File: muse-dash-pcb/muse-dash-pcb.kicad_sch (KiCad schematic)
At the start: 24 parts, among them SW0 CherryMX, SW1 CherryMX, SW1 SW_Push, SW2 CherryMX, SW3 CherryMX, U1 ATmega32U4-A, Y1 Crystal_GND24

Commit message: added footprints
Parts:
- C1: renamed from C2; footprint (none) -> Capacitor_SMD:C_0805_2012Metric
- C2: renamed from C6; footprint (none) -> Capacitor_SMD:C_0805_2012Metric
- C3: renamed from C7; footprint (none) -> Capacitor_SMD:C_0805_2012Metric
- C4: renamed from C3; footprint (none) -> Capacitor_SMD:C_0805_2012Metric
- C5: renamed from C4; footprint (none) -> Capacitor_SMD:C_0805_2012Metric
- C6: renamed from C1; footprint (none) -> Capacitor_SMD:C_0805_2012Metric
- C7: renamed from C5; footprint (none) -> Capacitor_SMD:C_0805_2012Metric
- D1: footprint (none) -> Diode_SMD:D_0805_2012Metric_Pad1.15x1.40mm_HandSolder
- D2: renamed from D3; footprint (none) -> Diode_SMD:D_0805_2012Metric_Pad1.15x1.40mm_HandSolder
- D3: renamed from D4; footprint (none) -> Diode_SMD:D_0805_2012Metric_Pad1.15x1.40mm_HandSolder
- D4: renamed from D2; footprint (none) -> Diode_SMD:D_0805_2012Metric_Pad1.15x1.40mm_HandSolder
- F1: footprint (none) -> Fuse:Fuse_1206_3216Metric_Pad1.42x1.75mm_HandSolder
- R1: renamed from R2; footprint (none) -> Resistor_SMD:R_0805_2012Metric_Pad1.20x1.40mm_HandSolder
- R2: renamed from R3; footprint (none) -> Resistor_SMD:R_0805_2012Metric_Pad1.20x1.40mm_HandSolder
- R3: renamed from R4; footprint (none) -> Resistor_SMD:R_0805_2012Metric_Pad1.20x1.40mm_HandSolder
- R4: renamed from R1; footprint (none) -> Resistor_SMD:R_0805_2012Metric_Pad1.20x1.40mm_HandSolder
- SW0: renamed from SW1; footprint (none) -> Button_Switch_SMD:SW_SPST_SKQG_WithStem
- SW1: renamed from SW0; footprint (none) -> Button_Switch_Keyboard:SW_Cherry_MX_1.00u_PCB
- SW2: renamed from SW1; footprint (none) -> Button_Switch_Keyboard:SW_Cherry_MX_1.00u_PCB
- SW3: renamed from SW2; footprint (none) -> Button_Switch_Keyboard:SW_Cherry_MX_1.00u_PCB
- SW4: renamed from SW3; footprint (none) -> Button_Switch_Keyboard:SW_Cherry_MX_1.00u_PCB
- Y1: footprint (none) -> Crystal:Crystal_SMD_3225-4Pin_3.2x2.5mm_HandSoldering
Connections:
- net SW1: now also U1.10 (PB2); no longer SW2.2, U1.11 (PB3)
- net SW2: now also SW2.2, U1.11 (PB3); no longer SW3.2, U1.28 (PB4)
- net SW3: now also SW3.2, U1.28 (PB4); no longer U1.29 (PB5)
- net SW0 renamed SW4
- net SW4: now also U1.29 (PB5); no longer U1.10 (PB2)

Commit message: completed pcb design
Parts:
- USB1: footprint (none) -> Connector_USB:USB_Mini-B_Lumberg_2486_01_Horizontal
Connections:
- net COM: now also U1.22 (PD5)
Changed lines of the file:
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@@
+		)
+	)
+	(global_label "COM"
+		(shape input)
+		(at 91.44 132.08 0)
+		(fields_autoplaced yes)
+		(effects
+			(font
+				(size 1.27 1.27)
+			)
+			(justify left)
+		)
+		(property "Intersheetrefs" "${INTERSHEET_REFS}"
+			(at 98.4771 132.08 0)
+			(effects
+				(font
+					(size 1.27 1.27)
+				)
+				(justify left)
+				(hide yes)
+			)
 		)
 	)
@@
 			)
 		)
-		(property "Footprint" ""
+		(property "Footprint" "Connector_USB:USB_Mini-B_Lumberg_2486_01_Horizontal"
 			(at 238.76 34.29 0)
 			(effects

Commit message: fixed routes and added mounting holes
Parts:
- added H1, H2, H3, H4: MountingHole, MountingHole:MountingHole_2.1mm, symbol Mechanical:MountingHole

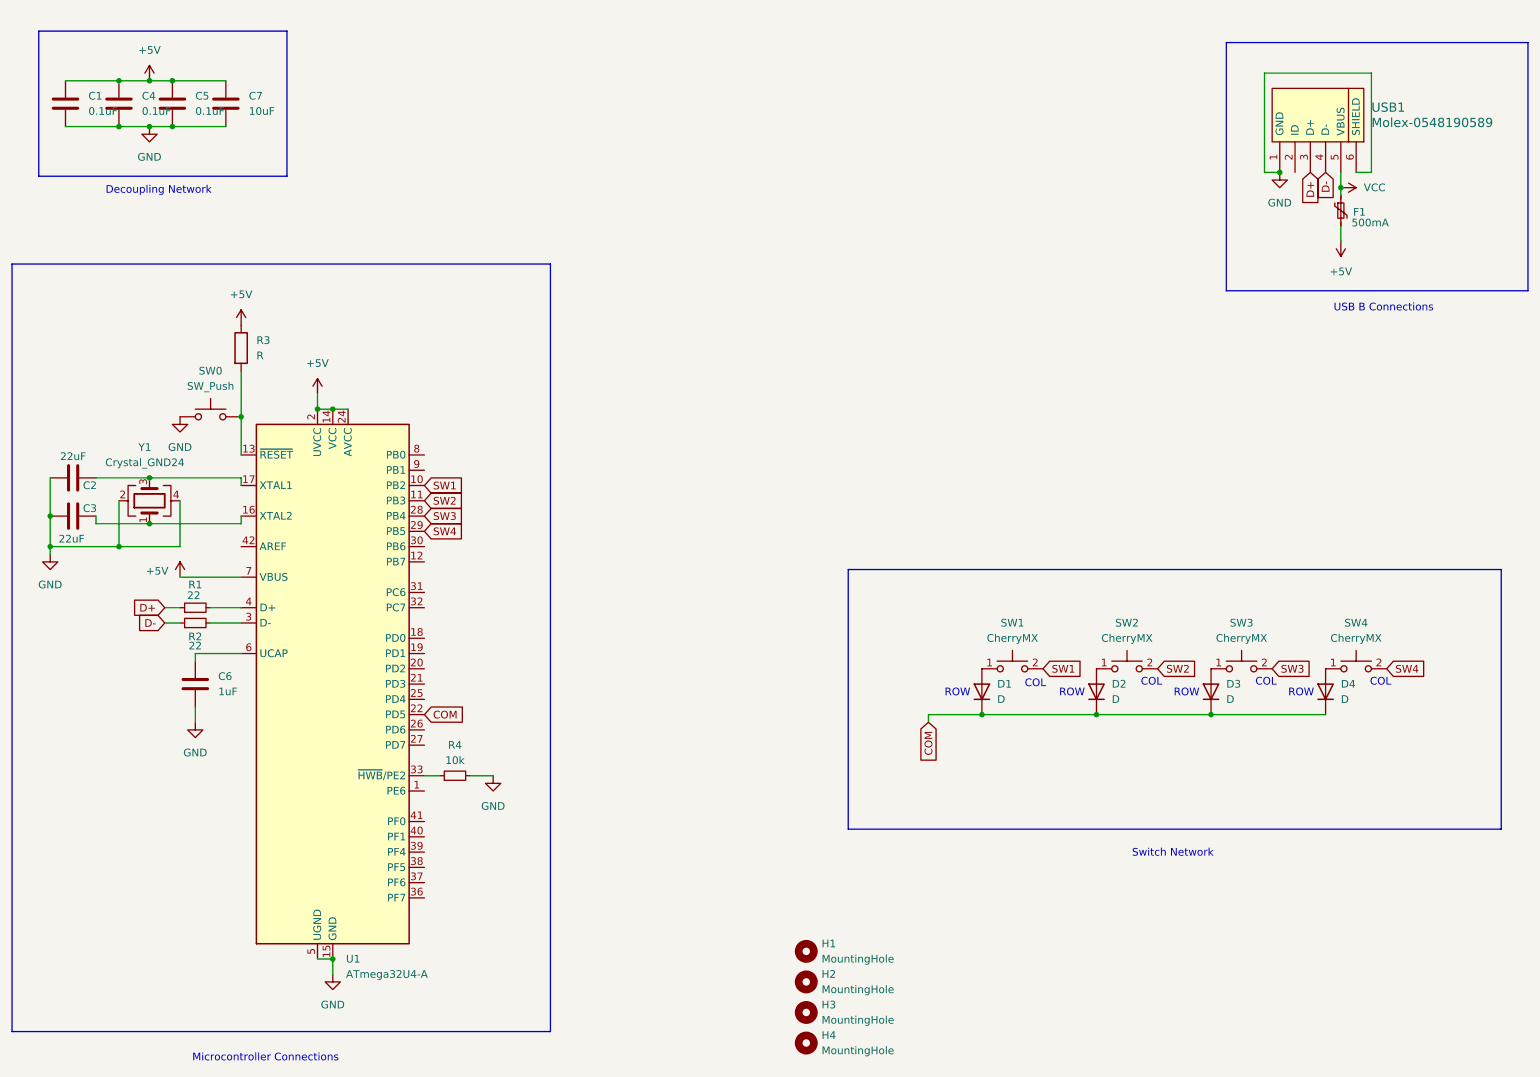
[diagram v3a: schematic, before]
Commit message: added ISP Interface
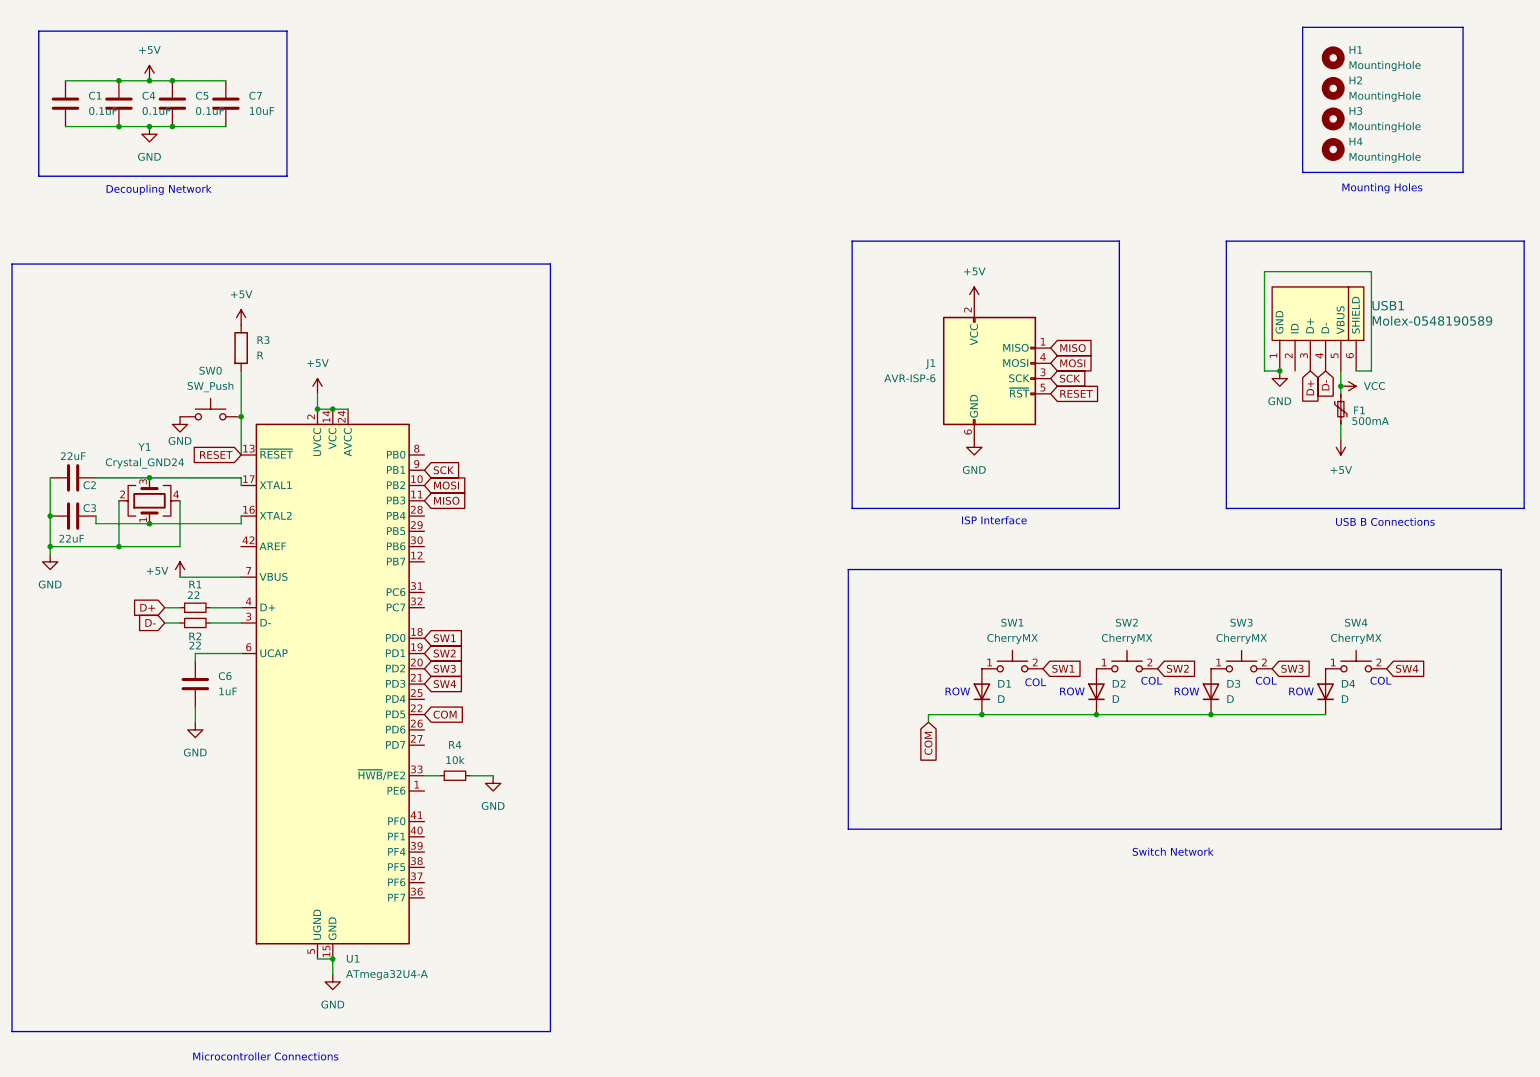
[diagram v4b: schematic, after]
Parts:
- added J1: AVR-ISP-6, Connector_PinHeader_1.00mm:PinHeader_2x03_P1.00mm_Vertical, symbol Connector:AVR-ISP-6
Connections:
- net +5V: now also J1.2 (VCC)
- net GND: now also J1.6 (GND)
- net SW1: now also U1.18 (PD0); no longer U1.10 (PB2)
- net SW2: now also U1.19 (PD1); no longer U1.11 (PB3)
- net SW3: now also U1.20 (PD2); no longer U1.28 (PB4)
- net SW4: now also U1.21 (PD3); no longer U1.29 (PB5)
- net RESET: now reaches R3.2, SW0.2, U1.13 (~{RESET})
- net RESET: now also J1.5 (~{RST})
- net SCK: now reaches U1.9 (PB1)
- net SCK: now also J1.3 (SCK)
- new net MISO: J1.1 (MISO), U1.11 (PB3)
- new net MOSI: J1.4 (MOSI), U1.10 (PB2)
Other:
- note added: "ISP Interface"
- note added: "Mounting Holes"
- moved on the sheet: F1, H1, H2, H3, H4, USB1

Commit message: added underglow LEDs
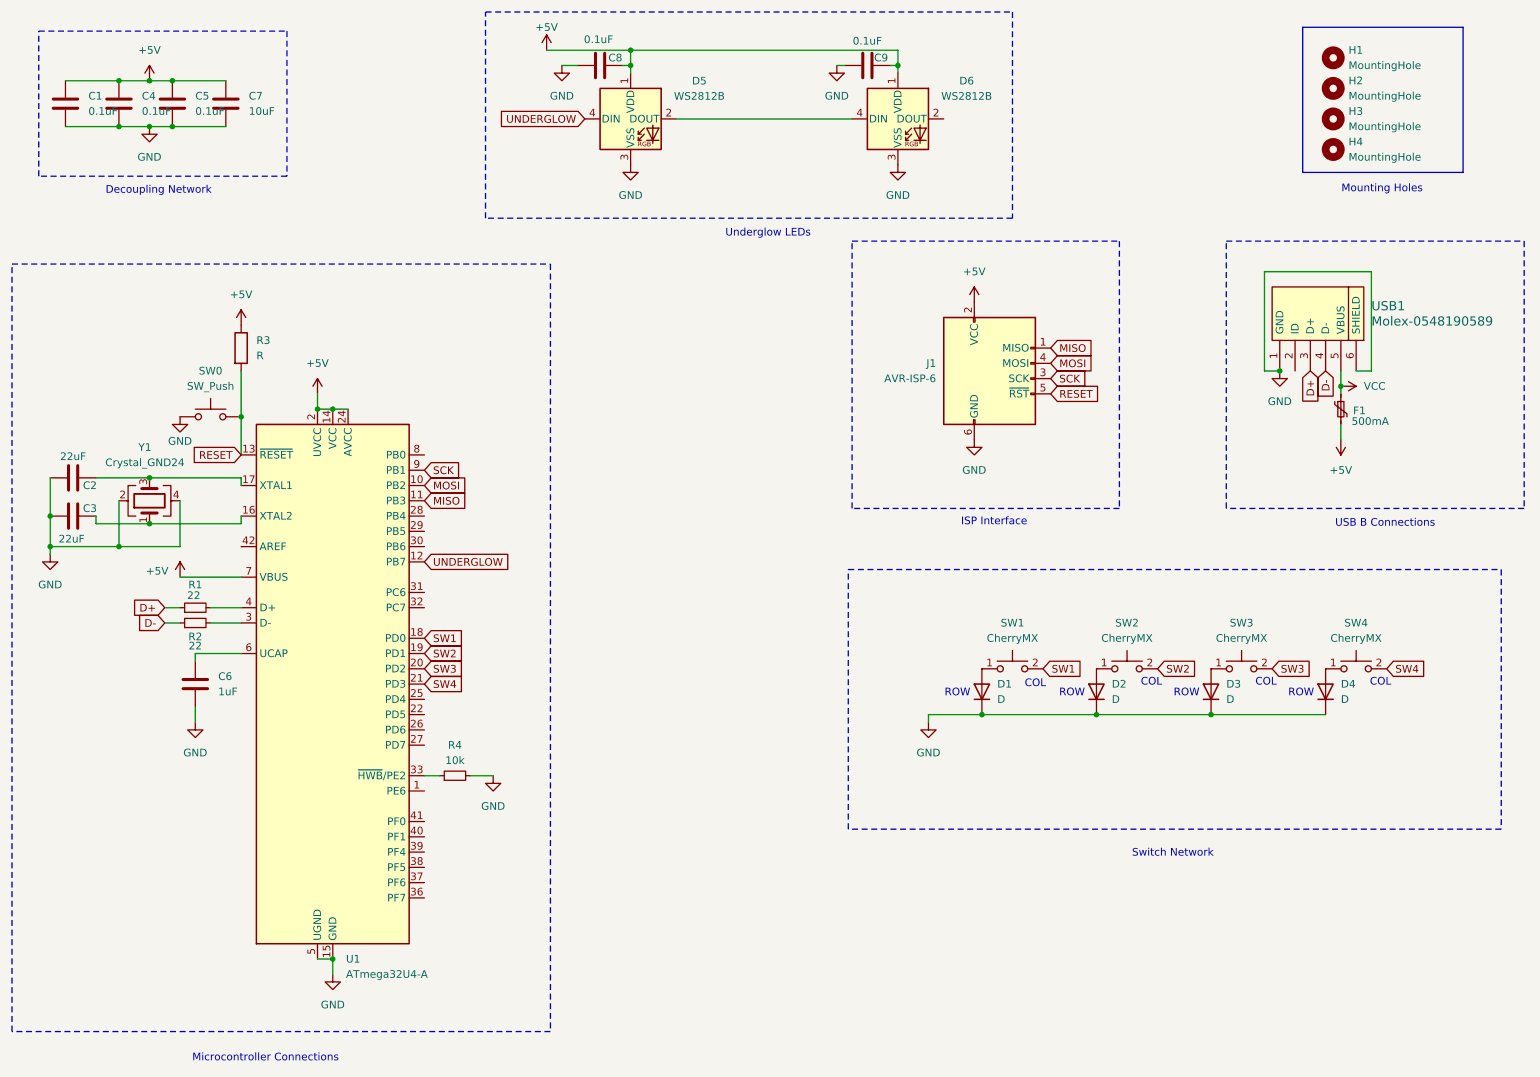
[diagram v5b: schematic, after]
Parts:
- added C8, C9: 0.1uF, Capacitor_SMD:C_0805_2012Metric, symbol Device:C
- added D5, D6: WS2812B, LED_SMD:LED_WS2812B_PLCC4_5.0x5.0mm_P3.2mm, symbol LED:WS2812B
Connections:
- net +5V: now also C8.2, C9.1, D5.1 (VDD), D6.1 (VDD)
- net GND: now also D1.1 (K), D2.1 (K), D3.1 (K), D4.1 (K), C8.1, C9.2, D5.3 (VSS), D6.3 (VSS)
- net UNDERGLOW: now reaches U1.12 (PB7)
- net UNDERGLOW: now also D5.4 (DIN)
- removed net COM: D1.1 (K), D2.1 (K), D3.1 (K), D4.1 (K), U1.22 (PD5)
- new net: D5.2 (DOUT), D6.4 (DIN)
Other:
- note added: "Underglow LEDs"

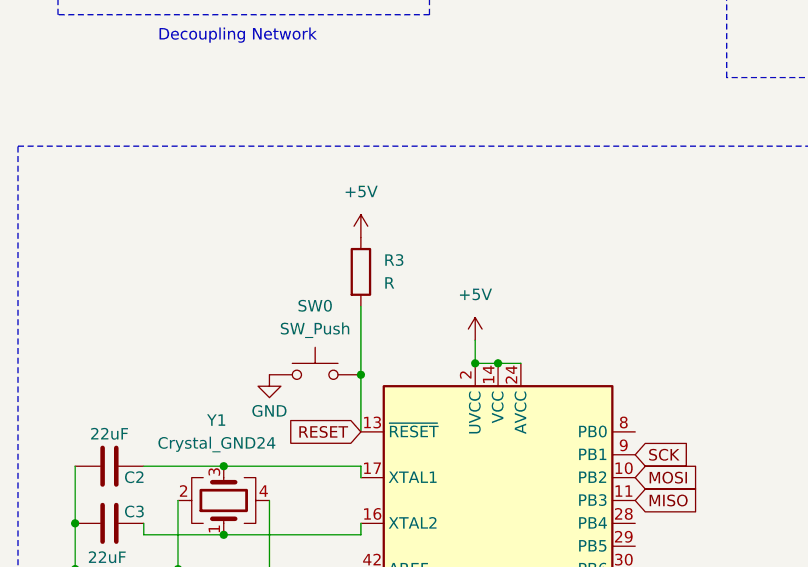
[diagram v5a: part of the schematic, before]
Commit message: added missing resistor value
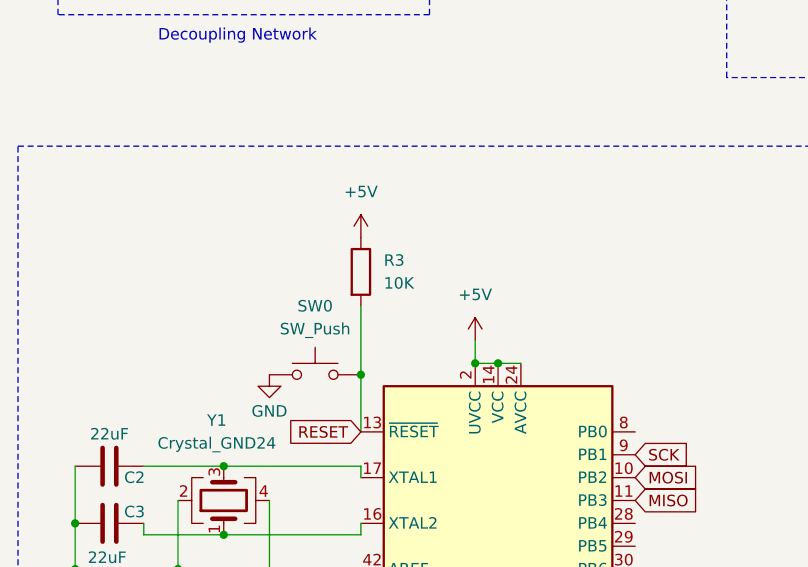
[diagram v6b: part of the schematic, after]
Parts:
- R3: value R -> 10K
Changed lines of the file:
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@@
 			)
 		)
-		(property "Value" "R"
+		(property "Value" "10K"
 			(at 63.5 72.3899 0)
 			(effects

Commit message: changed ISP header footprint, fixed Ground plane and improved routing
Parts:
- J1: footprint Connector_PinHeader_1.00mm:PinHeader_2x03_P1.00mm_Vertical -> Connector_PinHeader_2.54mm:PinHeader_2x03_P2.54mm_Vertical
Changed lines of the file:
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@@
 			)
 		)
-		(property "Footprint" "Connector_PinHeader_1.00mm:PinHeader_2x03_P1.00mm_Vertical"
+		(property "Footprint" "Connector_PinHeader_2.54mm:PinHeader_2x03_P2.54mm_Vertical"
 			(at 179.07 74.93 90)
 			(effects

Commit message: changed oscillator footprint
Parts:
- Y1: footprint Crystal:Crystal_SMD_3225-4Pin_3.2x2.5mm_HandSoldering -> Crystal:Crystal_SMD_HC49-SD
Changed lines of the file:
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@@
 			)
 		)
-		(property "Footprint" "Crystal:Crystal_SMD_3225-4Pin_3.2x2.5mm_HandSoldering"
+		(property "Footprint" "Crystal:Crystal_SMD_HC49-SD"
 			(at 45.72 96.52 0)
 			(effects
